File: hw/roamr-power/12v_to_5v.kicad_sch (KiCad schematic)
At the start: 18 parts, among them U1 TPS56A37RPAR

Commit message: reorganizing to roamr-power
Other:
- title: (none) -> ROAMR power board
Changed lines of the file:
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@@
 	(generator_version "9.0")
 	(paper "USLetter")
+	(title_block
+		(title "ROAMR power board")
+		(date "2026-01-18")
+		(rev "1.0")
+	)
 	(text "Leaving EN floating \nenables the device"
 		(exclude_from_sim no)

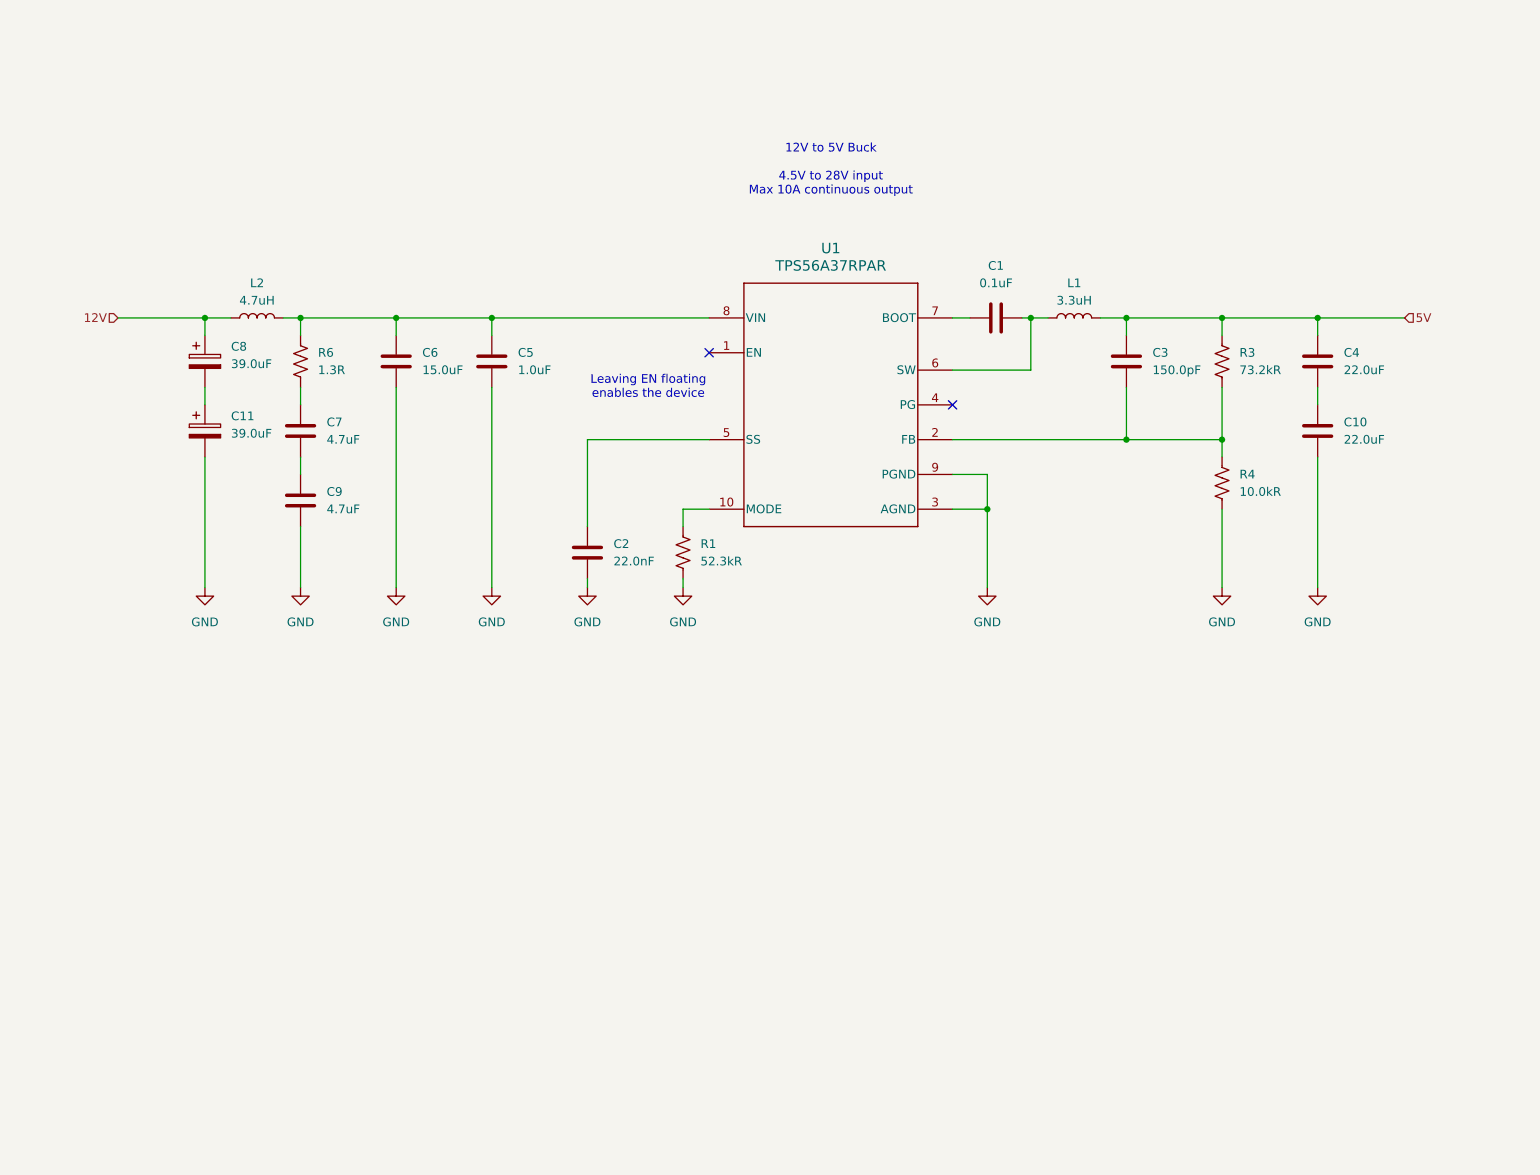
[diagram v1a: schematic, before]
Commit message: mostly finished power, probably need a bit of drawing cleanup, for schematic
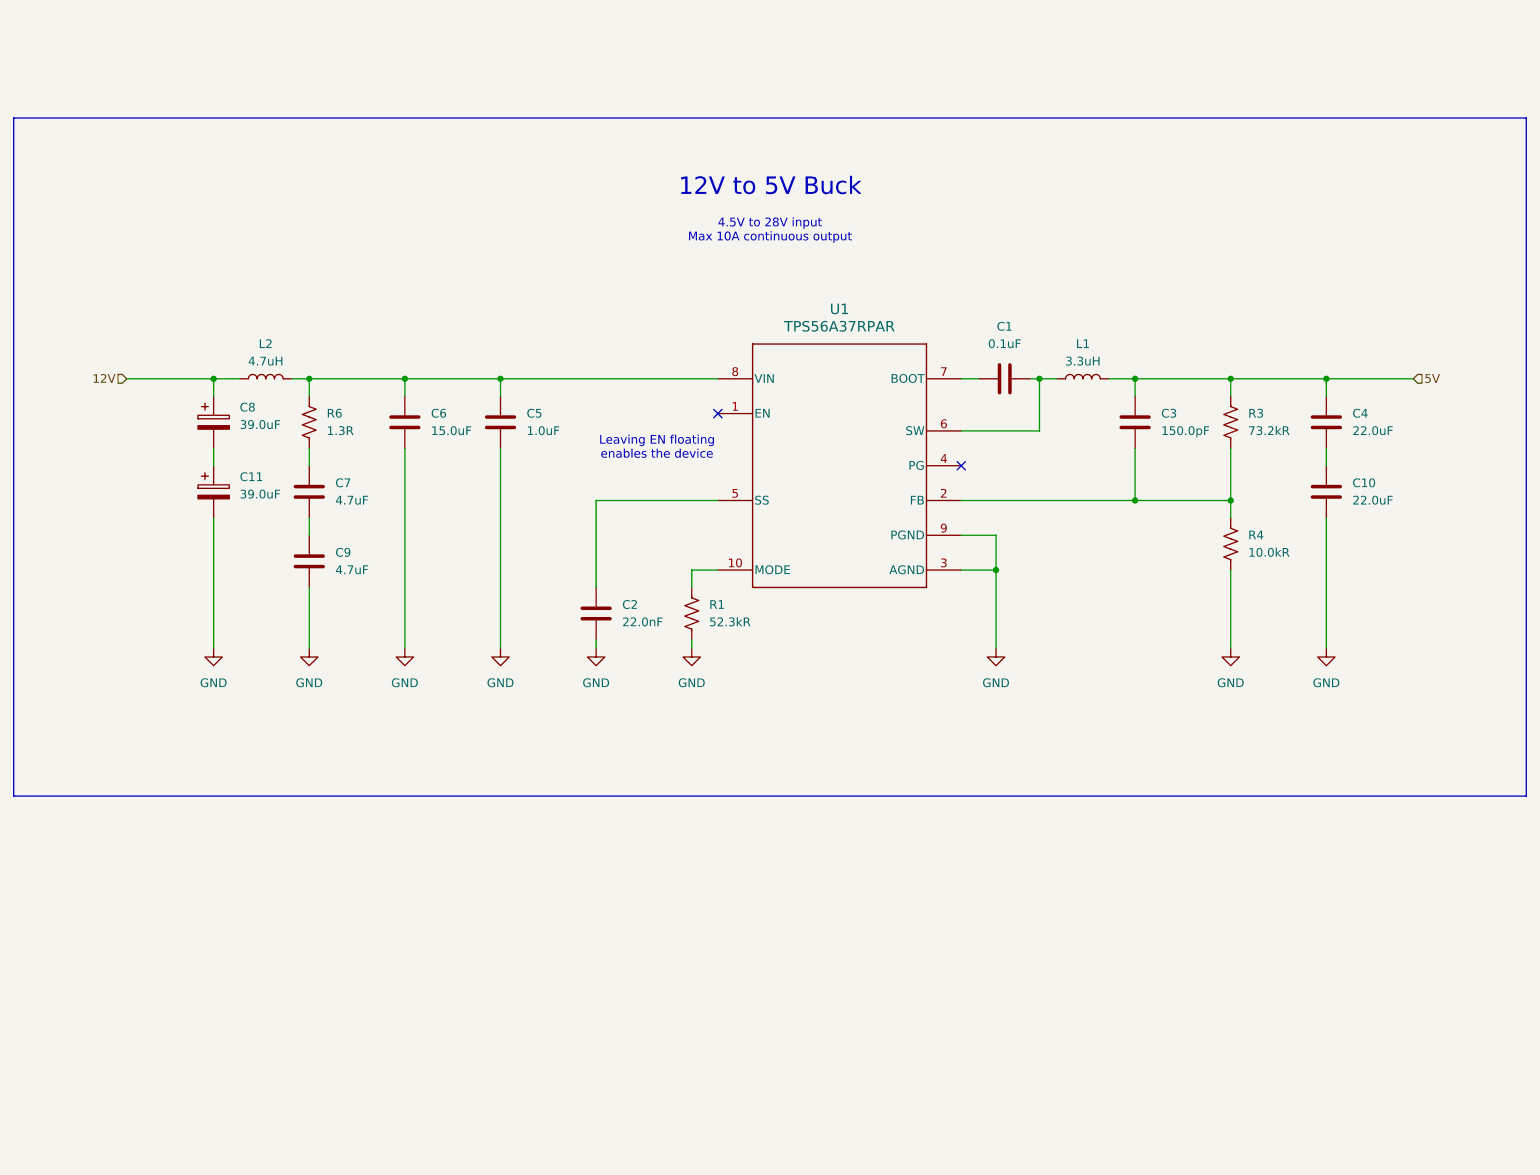
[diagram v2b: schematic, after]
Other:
- note added: "12V to 5V Buck"
- note added: "4.5V to 28V input Max 10A continuous output"
- note removed: "12V to 5V Buck 4.5V to 28V input Max 10A continuous output"
- moved on the sheet: C1, C10, C11, C2, C3, C4, C5, C6, C7, C8, C9, L1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

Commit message: fixed after nathan's rereview
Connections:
- net 12V renamed +12V
- net 5V renamed +5V
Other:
- company: (none) -> Mechatronics FYDP Group 16

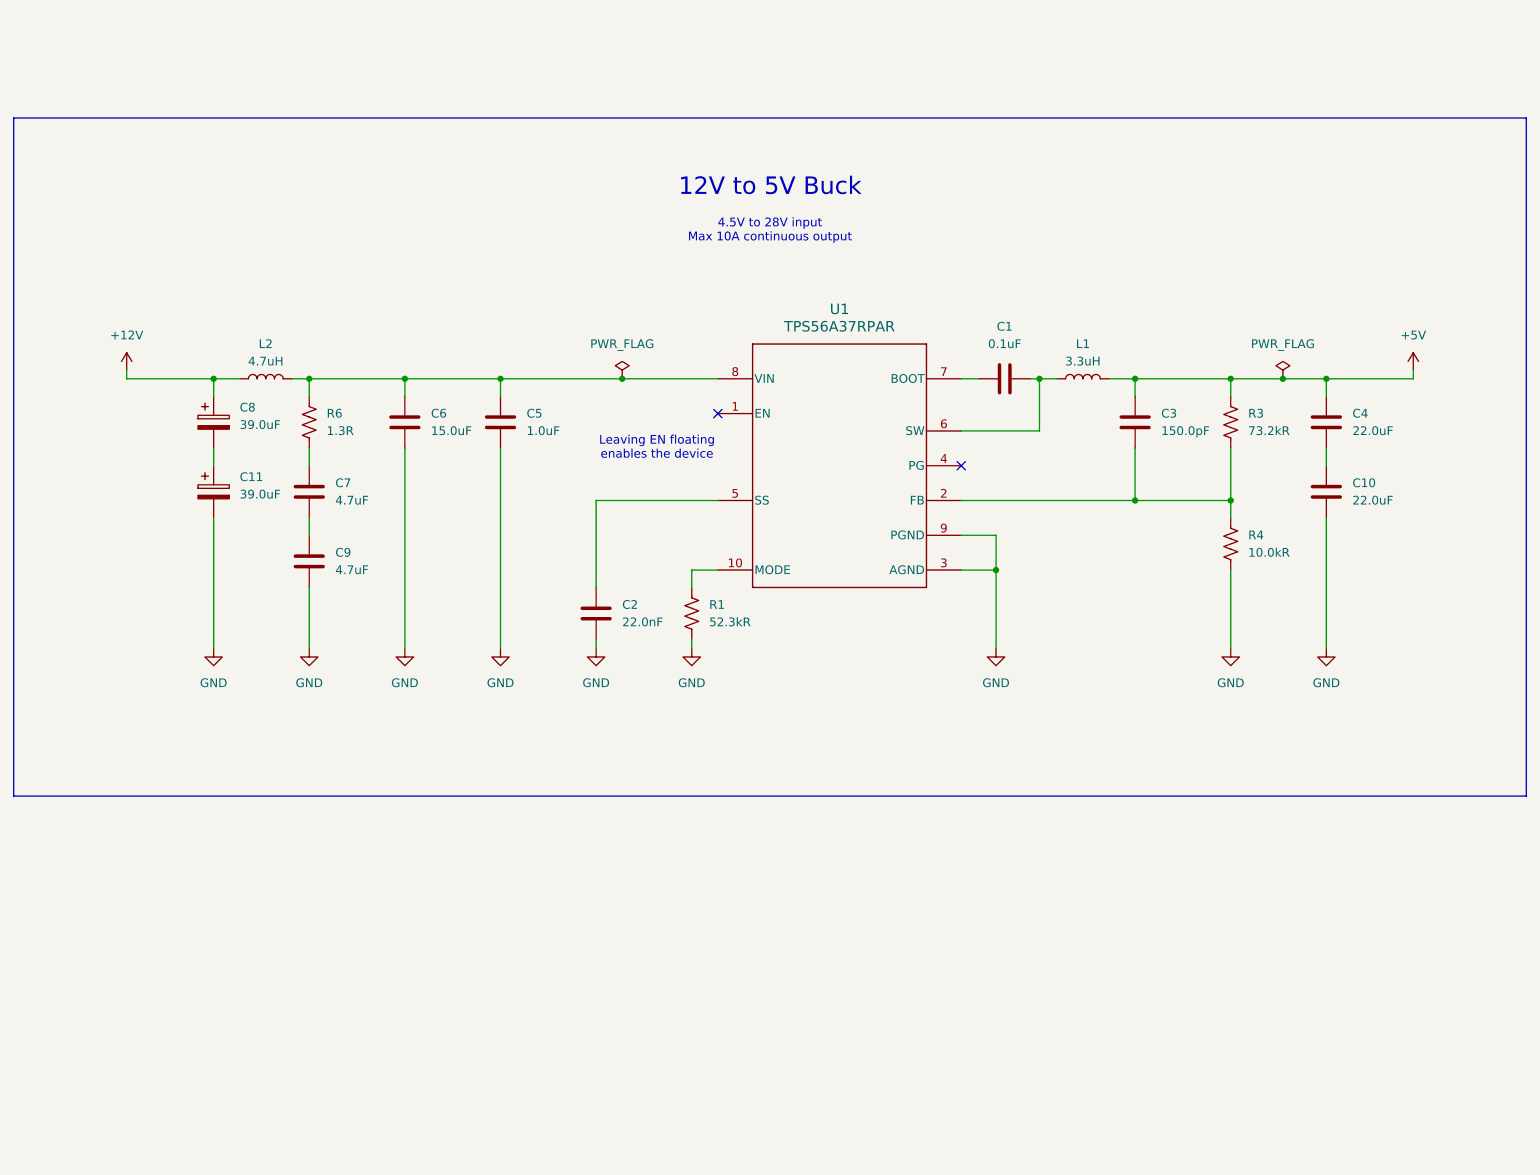
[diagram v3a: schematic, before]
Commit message: picked the BOM and added two more indicator LEDs for the 12V and 5V rails
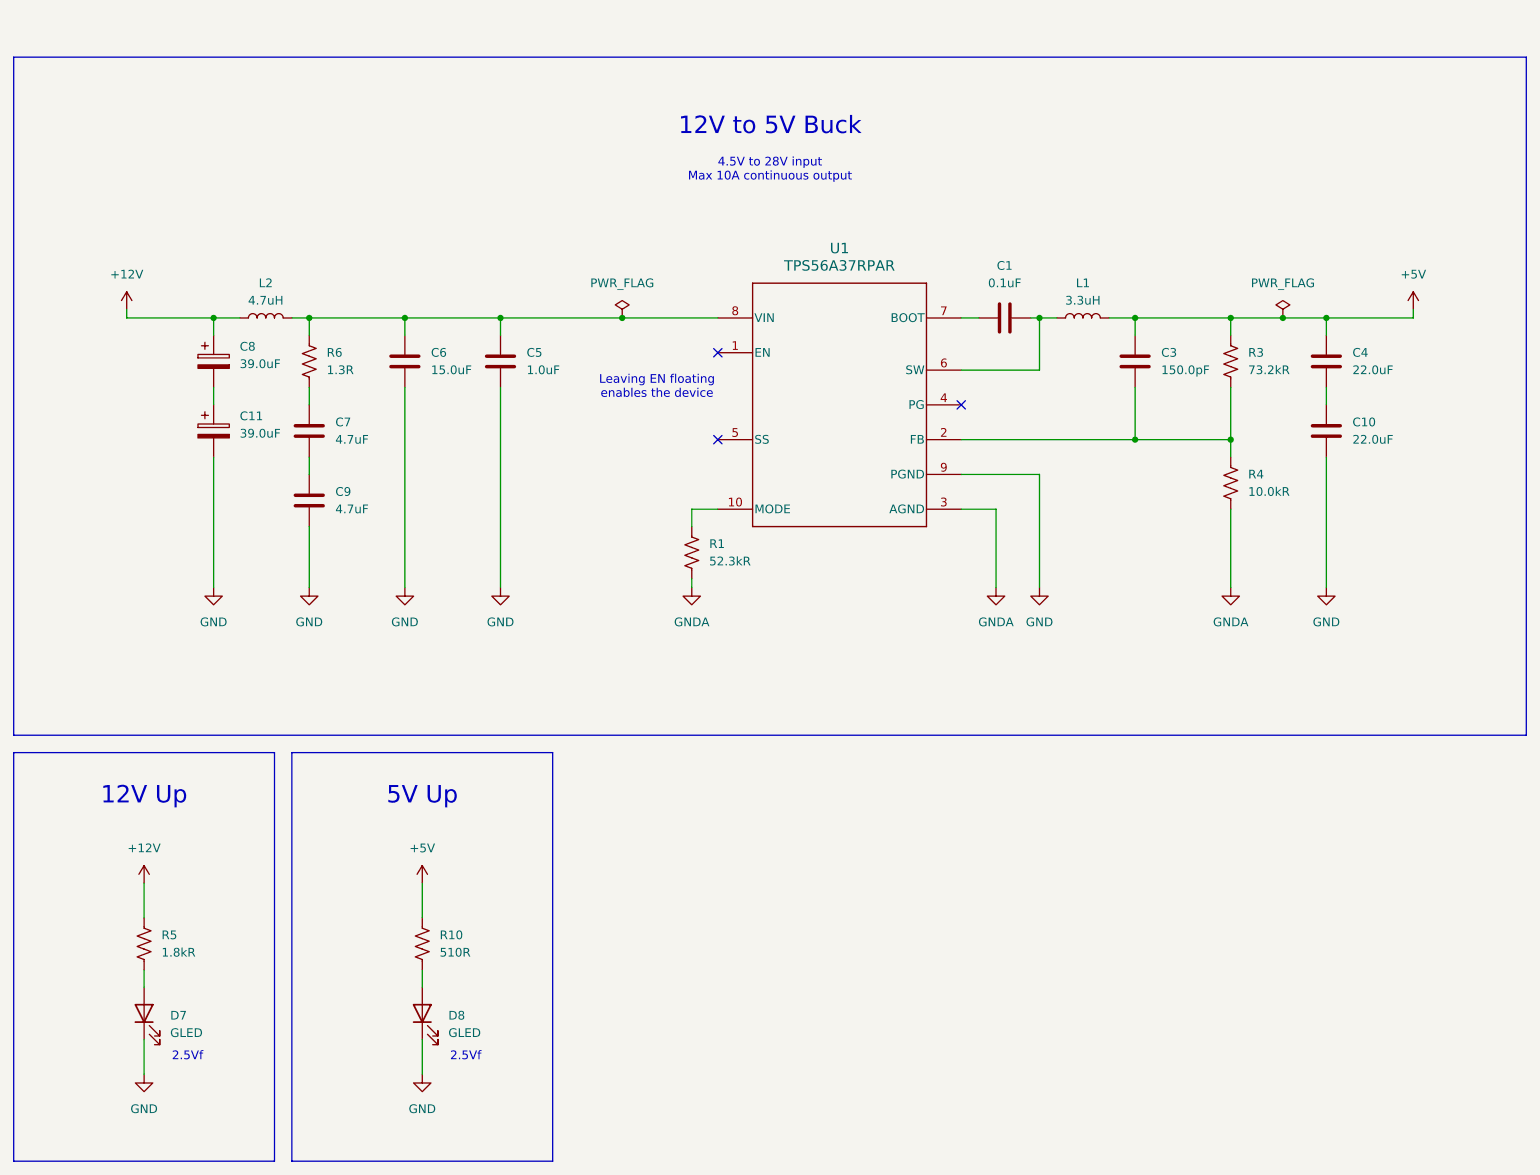
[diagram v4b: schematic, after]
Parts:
- removed C2: 22.0nF, symbol Device:C
- added D7, D8: GLED, KT_EELP41.12-S2U1-25-2X4X-5-R18:KTEELP4112S2U1252X4X5R18, symbol Device:LED
- added R10: 510R, Resistor_SMD:R_0603_1608Metric, symbol Device:R_US
- added R5: 1.8kR, Resistor_SMD:R_0603_1608Metric, symbol Device:R_US
- C1, C10, C3, C4, C5, C6, C7, C9: footprint (none) -> Capacitor_SMD:C_0603_1608Metric
- C11, C8: footprint (none) -> 35SVPF39M:16SVF270M
- L1: footprint (none) -> ETQ-P4M3R3YFN:IND_PCC-M0645M_PAN-L
- L2: footprint (none) -> VLS6045EX_4R7M:IND_VLS6045EX-4R7M_TDK-L
- R1, R3, R4, R6: footprint (none) -> Resistor_SMD:R_0603_1608Metric
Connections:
- net +12V: now also R5.1
- net +5V: now also R10.1
- net GND: now also D7.1 (K), D8.1 (K); no longer R1.1, R4.1, U1.3 (AGND)
- new net: D7.2 (A), R5.2
- new net: D8.2 (A), R10.2
- new net GNDA: R1.1, R4.1, U1.3 (AGND)
- no-connect marks 2 -> 3
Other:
- note added: "12V Up"
- note added: "2.5Vf"
- note added: "5V Up"
- moved on the sheet: C1, C10, C11, C3, C4, C5, C6, C7, C8, C9, L1, L2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

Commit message: layout
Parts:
- added NT1: NetTie_2, NetTie:NetTie-2_SMD_Pad0.5mm, symbol Device:NetTie_2
- L2: footprint VLS6045EX_4R7M:IND_VLS6045EX-4R7M_TDK-L -> VLS6045EX_4R7M:IND_VLS6045EX-4R7M_TDK
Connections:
- net +12V: now also C11.1
- net +5V: now also C10.1
- net GND: now also C4.2, C7.2, C8.2, NT1.2
- net GNDA: now also NT1.1
- net SW_OUT: now reaches C1.2, L1.1, U1.6 (SW)
- net 12V_SW: now reaches C5.1, C6.1, L2.2, R6.1, U1.8 (VIN)
- net at C7.1, R6.2: now also C9.1
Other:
- moved on the sheet: C10, C11, C7, C9

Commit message: pcb schematic and layout updated
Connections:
- net +12V renamed VSYS_12V
- net +5V renamed VSYS_5V
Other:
- moved on the sheet: C1, C10, C11, C3, C4, C5, C6, C7, C8, C9, D7, D8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

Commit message: final edits
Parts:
- C6: footprint Capacitor_SMD:C_0603_1608Metric -> Capacitor_SMD:C_0805_2012Metric
- D7, D8: footprint KT_EELP41.12-S2U1-25-2X4X-5-R18:KTEELP4112S2U1252X4X5R18 -> KT-0603:LEDC1608X70N; Manufacturer_Part_Number (none) -> KT-0603G
- L1: Manufacturer_Part_Number (none) -> ETQ-L4M3R3YFN
- L2: Manufacturer_Part_Number (none) -> VLS6045EX
- R10: value 510R -> 910R
- R5: value 1.8kR -> 4.3kR
- U1: Manufacturer_Part_Number (none) -> TPS56A37RPAR
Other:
- note added: "3.1Vf"
- note removed: "2.5Vf"
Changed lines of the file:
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@@
 		)
 	)
-	(text "2.5Vf"
+	(text "3.1Vf"
 		(exclude_from_sim no)
 		(at 54.61 175.26 0)
@@
 		)
 	)
-	(text "2.5Vf"
+	(text "3.1Vf\n"
 		(exclude_from_sim no)
 		(at 99.06 175.26 0)
@@
 			)
 		)
-		(property "Value" "1.8kR"
+		(property "Value" "4.3kR"
 			(at 50.8 160.0199 0)
 			(effects
@@
 			)
 		)
+		(property "Manufacturer_Part_Number" "VLS6045EX"
+			(at 66.04 64.77 90)
+			(effects
+				(font
+					(size 1.27 1.27)
+				)
+				(hide yes)
+			)
+		)
 		(pin "1"
 		)
@@
 			)
 		)
-		(property "Footprint" "KT_EELP41.12-S2U1-25-2X4X-5-R18:KTEELP4112S2U1252X4X5R18"
+		(property "Footprint" "KT-0603:LEDC1608X70N"
 			(at 48.26 168.91 0)
 			(effects
@@
 			)
 		)
+		(property "Manufacturer_Part_Number" "KT-0603G"
+			(at 48.26 168.91 90)
+			(effects
+				(font
+					(size 1.27 1.27)
+				)
+				(hide yes)
+			)
+		)
 		(pin "1"
 		)
@@
 			)
 		)
-		(property "Footprint" "Capacitor_SMD:C_0603_1608Metric"
+		(property "Footprint" "Capacitor_SMD:C_0805_2012Metric"
 			(at 87.3252 74.93 0)
 			(effects
@@
 			)
 		)
-		(property "Footprint" "KT_EELP41.12-S2U1-25-2X4X-5-R18:KTEELP4112S2U1252X4X5R18"
+		(property "Footprint" "KT-0603:LEDC1608X70N"
 			(at 92.71 168.91 0)
 			(effects
@@
 			)
 		)
+		(property "Manufacturer_Part_Number" "KT-0603G"
+			(at 92.71 168.91 90)
+			(effects
+				(font
+					(size 1.27 1.27)
+				)
+				(hide yes)
+			)
+		)
 		(pin "1"
 		)
@@
 			)
 		)
+		(property "Manufacturer_Part_Number" "TPS56A37RPAR"
+			(at 132.08 64.77 0)
+			(effects
+				(font
+					(size 1.27 1.27)
+				)
+				(hide yes)
+			)
+		)
 		(pin "3"
 		)
@@
 			)
 		)
+		(property "Manufacturer_Part_Number" "ETQ-L4M3R3YFN"
+			(at 185.42 64.77 90)
+			(effects
+				(font
+					(size 1.27 1.27)
+				)
+				(hide yes)
+			)
+		)
 		(pin "2"
 		)
@@
 			)
 		)
-		(property "Value" "510R"
+		(property "Value" "910R"
 			(at 95.25 160.0199 0)
 			(effects
